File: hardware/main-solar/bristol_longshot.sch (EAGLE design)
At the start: 84 parts, among them U1 SAM_D20E, U10 SPV1040, U11 LT4054ES5-4.2, U12 TPS62243, U13 TPS62243, U14 TPS3808, U15 74LVC1G04GW, U2 SI4060, U3 UBLOX_MAX, U4 SST25WF040BT-40I/NP, U5 TG-5006CJ, U6 TG-5006CJ, U7 TPS3123, U8 SN74LVC1G32DCKR, U9 SE880, Y1 ABS05

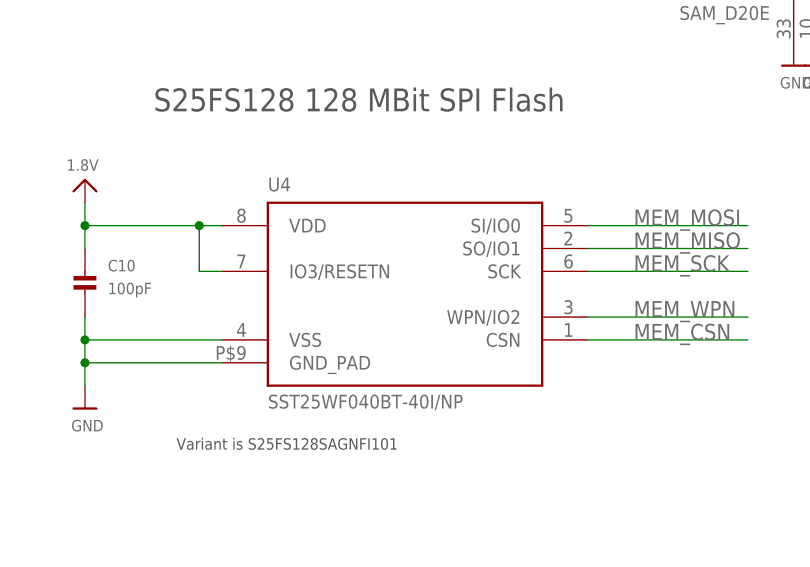
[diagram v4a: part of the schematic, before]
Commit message: Fixed memory pin names to correspond with the datasheet
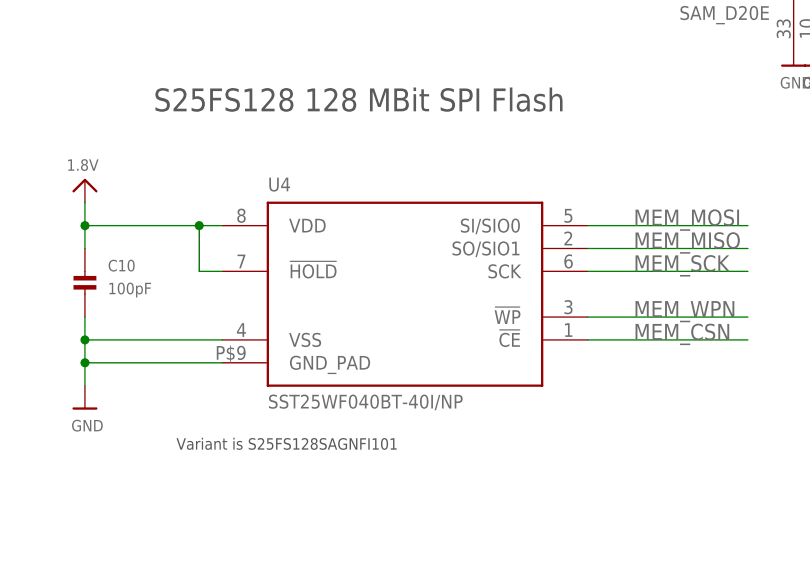
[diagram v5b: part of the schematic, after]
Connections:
- net 1.8V: now also U4.!HOLD; no longer U4.IO3/RESETN
- net MEM_CSN: now also U4.!CE; no longer U4.CSN
- net MEM_MISO: now also U4.SO/SIO1; no longer U4.SO/IO1
- net MEM_MOSI: now also U4.SI/SIO0; no longer U4.SI/IO0
- net MEM_WPN: now also U4.!WP; no longer U4.WPN/IO2
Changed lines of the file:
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@@
 <junction x="66.04" y="33.02"/>
 <pinref part="U4" gate="G$1" pin="VDD"/>
-<pinref part="U4" gate="G$1" pin="IO3/RESETN"/>
+<pinref part="U4" gate="G$1" pin="!HOLD"/>
 <wire x1="81.28" y1="27.94" x2="78.74" y2="27.94" width="0.1524" layer="91"/>
 <wire x1="78.74" y1="27.94" x2="78.74" y2="33.02" width="0.1524" layer="91"/>
@@
 <wire x1="121.92" y1="33.02" x2="139.7" y2="33.02" width="0.1524" layer="91"/>
 <label x="127" y="33.02" size="1.778" layer="95" ratio="11"/>
-<pinref part="U4" gate="G$1" pin="SI/IO0"/>
+<pinref part="U4" gate="G$1" pin="SI/SIO0"/>
 </segment>
 <segment>
@@
 <wire x1="139.7" y1="20.32" x2="121.92" y2="20.32" width="0.1524" layer="91"/>
 <label x="127" y="20.32" size="1.778" layer="95" ratio="11"/>
-<pinref part="U4" gate="G$1" pin="CSN"/>
+<pinref part="U4" gate="G$1" pin="!CE"/>
 </segment>
 <segment>
@@
 <wire x1="121.92" y1="22.86" x2="139.7" y2="22.86" width="0.1524" layer="91"/>
 <label x="127" y="22.86" size="1.778" layer="95" ratio="11"/>
-<pinref part="U4" gate="G$1" pin="WPN/IO2"/>
+<pinref part="U4" gate="G$1" pin="!WP"/>
 </segment>
 </net>
@@
 <wire x1="121.92" y1="30.48" x2="139.7" y2="30.48" width="0.1524" layer="91"/>
 <label x="127" y="30.48" size="1.778" layer="95" ratio="11"/>
-<pinref part="U4" gate="G$1" pin="SO/IO1"/>
-</segment>
-<segment>
+<pinref part="U4" gate="G$1" pin="SO/SIO1"/>
+</segment>
+<segment>

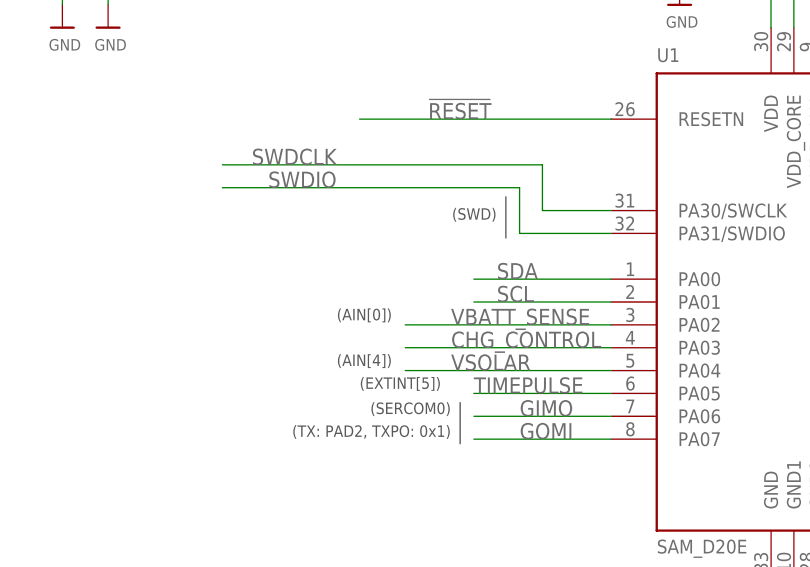
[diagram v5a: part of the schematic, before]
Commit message: Updated various sercom definitions
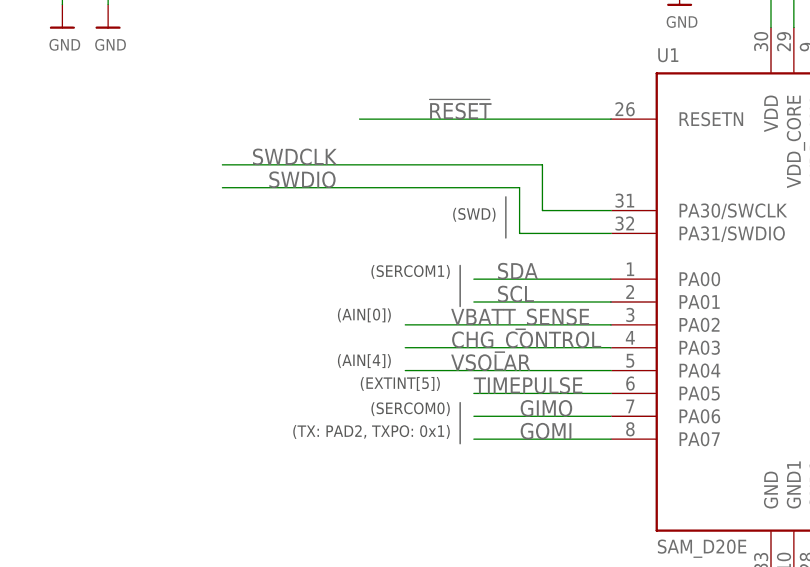
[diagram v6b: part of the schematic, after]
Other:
- note added: "(SERCOM1)"
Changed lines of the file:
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@@
 <text x="353.06" y="-35.56" size="1.778" layer="97">Place</text>
 <text x="165.1" y="-43.18" size="1.778" layer="97">4.25V = 1.25(180/75 + 1)</text>
+<wire x1="110.236" y1="87.884" x2="110.236" y2="83.312" width="0.1524" layer="97"/>
+<text x="109.22" y="86.614" size="1.27" layer="97" font="vector" ratio="11" rot="MR0">(SERCOM1)</text>
 </plain>
 <instances>

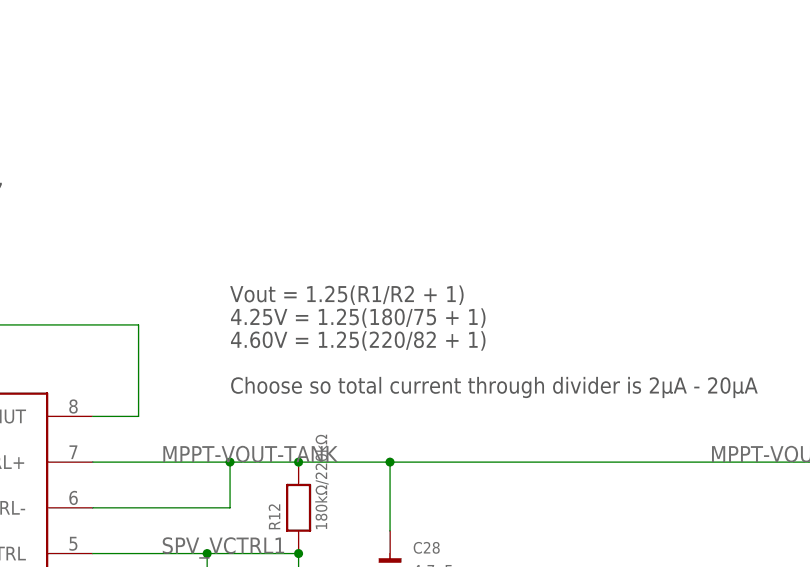
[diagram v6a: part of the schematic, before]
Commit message: Added vias though all the pads on the debug connector
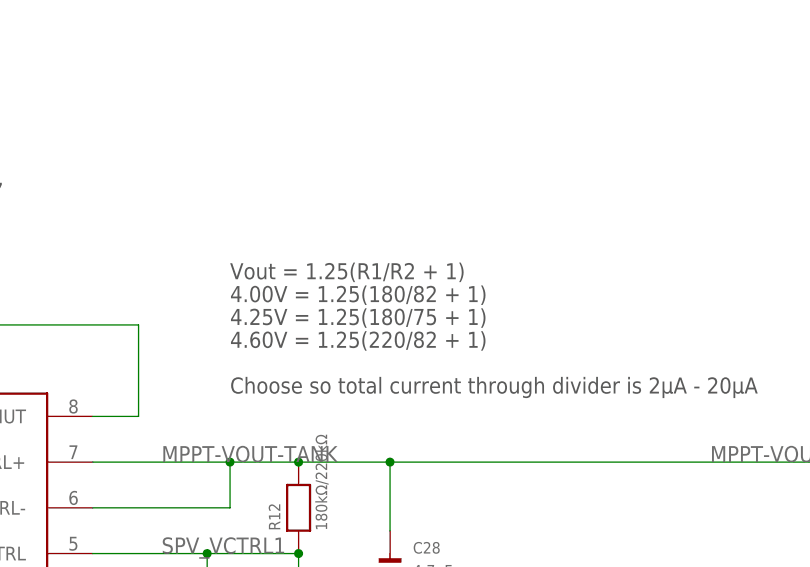
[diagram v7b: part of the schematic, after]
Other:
- note added: "4.00V = 1.25(180/82 + 1)"
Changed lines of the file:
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@@
 <text x="347.98" y="-114.3" size="1.778" layer="97">Rchg = 2.2kΩ gives Ichg = 70mA</text>
 <text x="347.98" y="-119.38" size="1.778" layer="97">Ichg can be measured by Vprog</text>
-<text x="165.1" y="-40.64" size="1.778" layer="97">Vout = 1.25(R1/R2 + 1)</text>
+<text x="165.1" y="-38.1" size="1.778" layer="97">Vout = 1.25(R1/R2 + 1)</text>
 <text x="165.1" y="-50.8" size="1.778" layer="97">Choose so total current through divider is 2µA - 20µA</text>
 <text x="7.62" y="-50.8" size="1.778" layer="97">Not actually an SMA connector</text>
@@
 <wire x1="110.236" y1="87.884" x2="110.236" y2="83.312" width="0.1524" layer="97"/>
 <text x="109.22" y="86.614" size="1.27" layer="97" font="vector" ratio="11" rot="MR0">(SERCOM1)</text>
+<text x="165.1" y="-40.64" size="1.778" layer="97">4.00V = 1.25(180/82 + 1)</text>
 </plain>
 <instances>

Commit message: Updated main tracker solar design to use a LTC3105 energy harvester for solar and a 3V primary lithium for backup. Work in Progress
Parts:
- removed C30, C31, C32: 4.7µF, microbuilder_v3:CAP_CERAMIC_0402
- removed C33, C35: 1nF, microbuilder_v3:CAP_CERAMIC_0402
- removed L1A: XAL6060, XAL6060:XAL6060
- removed L1B: 10uH LPS3015, PecanFemto4:IND-LPS3015
- removed L8, L9: 2.2µH, SparkFun:INDUCTOR1007
- removed R11: 1kΩ, microbuilder_v3:RESISTOR_0402
- removed R14: 2.2kΩ, microbuilder_v3:RESISTOR_0402
- removed R15: 0Ω/DNP, microbuilder_v3:RESISTOR_0402
- removed R6, R7: 10kΩ, microbuilder_v3:RESISTOR_0402
- removed U12, U13: TPS62243, TPS62243:TPS62243
- removed U14: TPS3808, TPS3808:TPS3808
- removed U15: 74LVC1G04GW, 74LVC1G04GW_inverter:74LVC1G04GW
- removed Y1: ABS05, fbri:ABS05
- added D1, U$46: RB161M, RB161M:RB161M
- added D5: (no value), microbuilder_v3:BAT54C
- added L1B1: 10uH LPS3015, PecanFemto4:IND-LPS3015
- C20: value 100nF -> 4.7µF
- C22: value 18pF -> 10µF; device microbuilder_v3:CAP_CERAMIC_0402 -> resistor:C-EUC0603K
- C23: value 18pF -> 1µF
- C25, C26: value 10µF -> 1µF; device resistor:C-EUC0603K -> microbuilder_v3:CAP_CERAMIC_0402
- C28: value 4.7µF -> 1µF
- C29: value 4.7µF -> 100nF
- C34: value 1nF -> 1µF
- D3, D4: value BAT760 -> RB161M; device BAT760:BAT760 -> RB161M:RB161M
- JTAG1: value M05 -> (none); device fbri:M05 -> microbuilder_v3:JTAG-CORTEXM3SMT
- R4: value 10kΩ -> 75kΩ
- U10: value SPV1040 -> LD6836TD/23P; device spv1040:SPV1040 -> LD6836TD_23:LD6836TD/23P
- U11: value LT4054ES5-4.2 -> TPS73118DBVT; device XYKlib:LT4054ES5-4.2 -> TPS73118DVBT:TPS73118DBVT
- U6: value TG-5006CJ -> LTC3105EDDPBF; device fbri:TG-5006CJ -> ltc3105:LTC3105EDDPBF
- U9: value SE880 -> BMP180; device fbri:SE880 -> SparkFun-Sensors:BMP180
- renumbered D2 to LED1
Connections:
- net LED2 renamed LED1
- removed net BATTERY_BUCK_SW: L8.1, U13.SW
- removed net BATTERY_EN: R7.1, U13.EN, U15.Y
- removed net CHG_STATUS: U11.CHRG
- removed net CT: U14.CT
- removed net LX1: L1A.2, L1B.2, U10.LX
- removed net MPP-SET: C33.P$2, R11.2, U10.MPP-SET
- removed net MPPT-VOUT-TANK: C28.P$1, C29.P$1, C31.P$1, D4.A, R12.2, R15.1, U10.ICTRL+, U10.ICTRL-, U10.VOUT, U11.VCC, U12.VIN, U14.SENSE
- removed net N$3: R3.2, U9.GPIO0
- removed net N$5: R2.2, U9.GPIO1
- removed net PROG: R14.2, U11.PROG
- removed net RTC_XI: C22.P$1, U9.RTC_XI, Y1.1
- removed net RTC_XO: C23.P$1, U9.RTC_XO, Y1.2
- removed net SE_MODE_PULL: R4.1, U9.CTS_SPI
- removed net SE_ON_OFF: U1.PA15, U9.ON_OFF
- removed net SE_TCXO_CLK: U6.OUT, U9.TCXO_CLK
- removed net SE_VCO_TCXO: C20.P$1, U6.VCC, U9.VCC_TCXO
- removed net SE_VREG: U9.VBB_I, U9.VREG_O
- removed net SPV_VCTRL1: C34.P$1, R12.1, R13.2, U10.VCTRL
- removed net SUPERVISOR_VCC: C35.P$1, D3.C, D4.C, R6.2, R7.2, U14.VDD, U15.VCC
- removed net TANK_BUCK_SW: L9.1, U12.SW
- removed net TANK_EN: R6.1, U12.EN, U14.!RESET, U15.A
- removed net VSOLAR: C24.1, C27.P$1, L1A.1, L1B.1, R11.1, U1.PA04, U10.XSHUT
- new net BATTERY_LDO_OUT: C25.P$1, D5.A2, U10.OUT
- new net BATTERY_P: C23.P$1, U10.EN, U10.IN
- new net GPS_!RESET: U1.PA15, U3.9_V_RESET
- new net MPPT_AUX: C34.P$1, U6.AUX
- new net MPPT_FB: R12.1, R13.2, U6.FB
- new net MPPT_LDO: C27.P$1, U6.LDO
- new net MPPT_SET: R4.2, U6.MPPC
- new net MPPT_SW: L1B1.2, U6.SW
- new net NR: C29.P$1, U11.NR/FB
- new net PANEL_1: D1.A
- new net PANEL_2: U$46.A
- new net PANEL_3: D3.A
- new net PANEL_4: D4.A
- new net SCHOTTY_COMB_OUT: C26.P$1, D5.C, U11.EN, U11.IN
- new net SOLAR: C24.1, D1.C, D3.C, D4.C, L1B1.1, U$46.C, U1.PA04, U6.VIN
- new net SOLAR_MPPT_OUT: C22.1, D5.A1, R12.2, U6.VOUT
- net !RESET: no longer U3.9_V_RESET, U9.NSRESET
- net 1.8V: now also C20.P$1, C28.P$1, JTAG1.1, R2.2, R3.2, U11.OUT, U9.VDDIO; no longer C25.1, C26.1, JTAG1.3, L8.2, L9.2, R4.2, U12.FB, U13.FB, U9.VKA
- net BATTERY: no longer C30.P$1, C32.P$1, D3.A, R15.2, U11.BAT, U13.VIN
- net CHG_CONTROL: no longer R14.1
- net EXT!RESET: now also JTAG1.10; no longer JTAG1.2
- net GIMO: no longer U9.RX
- net GND: now also C22.2, C25.P$2, C26.P$2, JTAG1.3, JTAG1.5, R4.1, U6.FBLDO, U9.GND; no longer C22.P$2, C25.2, C26.2, C30.P$2, C31.P$2, C32.P$2, C33.P$1, C35.P$2, JTAG1.1, R2.1, R3.1, U12.GND, U12.GND2, U12.MODE, U13.GND, U13.GND2, U13.MODE, U14.GND, U14.GND2, U15.GND, U9.GND1, U9.GND10, U9.GND2, U9.GND3, U9.GND4, U9.GND5, U9.GND6, U9.GND7, U9.GND8, U9.GND9
- net GOMI: no longer U9.TX
- net GPS_ANT: no longer U9.RF_IN
- net SCL: now also R2.1, U9.SCL
- net SDA: now also R3.1, U9.SDA
- net SWDCLK: now also JTAG1.4; no longer JTAG1.5
- net SWDIO: now also JTAG1.2; no longer JTAG1.4
- net TIMEPULSE: no longer U9.TM
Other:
- note added: "!SHDN! is pulled high internally, so converter is always enabled"
- note added: "0.8V - 1V from solar array"
- note added: "1.1V - 1.3V expected from two series solar cells at -25ºC"
- note added: "2.3V LDO"
- note added: "LDO output is set to 2.2V by default. Must be less that Vout."
- note added: "MPPT output set to 2.5V"
- note added: "MPPT set point is 0.75V"
- note added: "Single 3V primary lithium cell"
- note added: "Vf = 300mV @ -25ºC, 500mA"
- note added: "Vf = 500mV @ 100mA"
- note added: "Vldo = 20mV @ 100mA"
- note removed: "!MR! has internal pull-up"
- note removed: "4.00V = 1.25(180/82 + 1)"
- note removed: "4.25V = 1.25(180/75 + 1)"
- note removed: "4.60V = 1.25(220/82 + 1)"
- note removed: "Choose so total current through divider is 2µA - 20µA"
- note removed: "Enable: Vil = 0.4V, Vih=1V"
- note removed: "Ichg = 150V / Rchg"
- note removed: "Ichg can be measured by Vprog"
- note removed: "Input Voltage: 2 - 6V"
- note removed: "Leaving Ct open sets the reset time (transition battery->solar) to 20ms"
- note removed: "Not actually an SMA connector"
- note removed: "Place"
- note removed: "Rchg = 2.2kΩ gives Ichg = 70mA"
- note removed: "Recommended input cap is 1µF"
- note removed: "Still quite unsure on inductor value.. but 2.2µH is worth trying, since it would be much better than the recommended 10µH. Will the boost then run in inefficient discontinous mode????"
- note removed: "The ICTRL inputs are just pulled to Vout as we're not using constant-current regulation"
- note removed: "Undervoltage Lockout: 1.85V typ"
- note removed: "Undervoltage lockout for MPP-SET under 0.24V"
- note removed: "Vout = 1.25(R1/R2 + 1)"
- moved on the sheet: C19, C20, C22, C23, C24, C25, C26, C27, C28, C29, C34, R12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
